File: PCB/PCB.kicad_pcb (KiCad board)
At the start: 2 copper layers, 45.6 x 12.2 mm, 9 parts, among them U1 STM8S003F3P, U2 PCB-USB-PWR-connector, U3 D168K

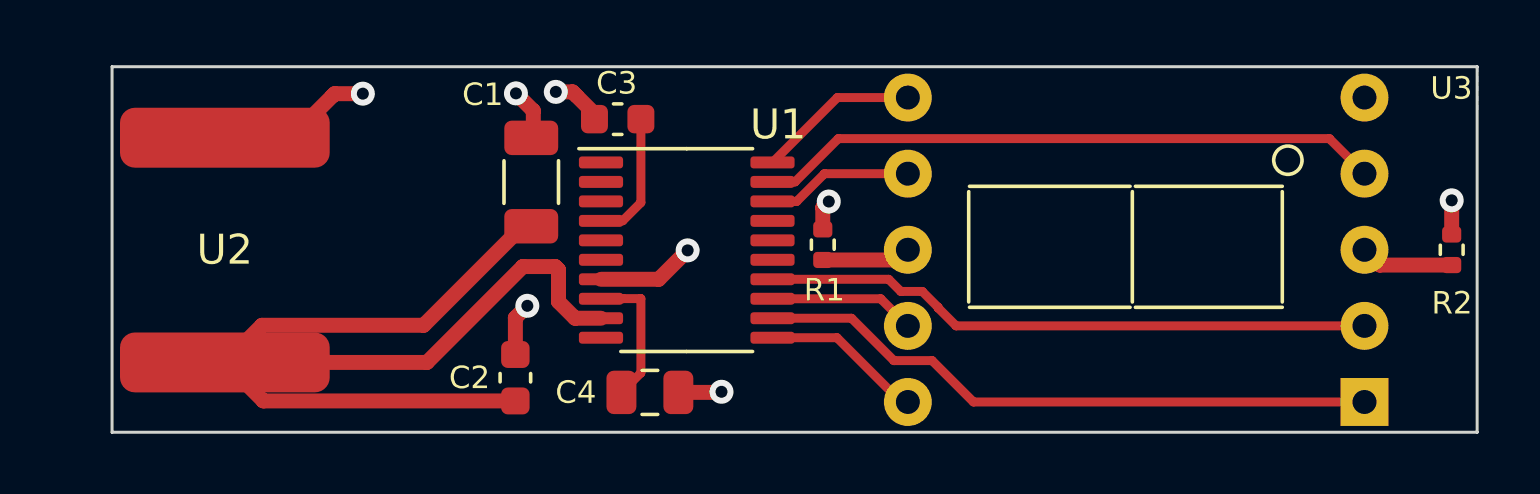
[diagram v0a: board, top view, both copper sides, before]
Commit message: PCB revision 0.11: correct decoupling capacitors, change IO routing, Schematic revision 0.12: change IO routing
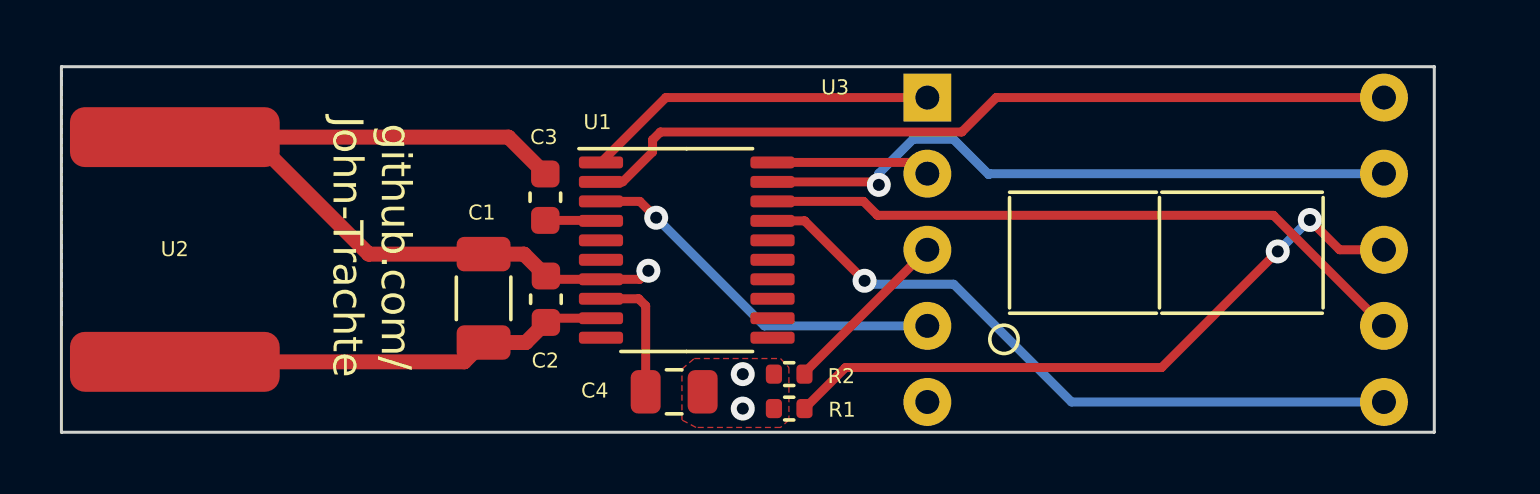
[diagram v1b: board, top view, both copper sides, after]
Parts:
- moved R2 22.5 mm to (153.0, 98.1), turned to 180 degrees
- moved U3 17.8 mm to (157.6, 88.9), turned to 0 degrees
- moved R1 5.58 mm to (153.0, 99.2), turned to 180 degrees
- moved C1 4.19 mm to (142.8, 95.6)
- moved C3 3.55 mm to (144.9, 92.2), turned to 90 degrees
- moved C2 2.81 mm to (144.9, 95.6)
- moved U2 1.67 mm to (132.5, 93.9)
- moved C4 0.81 mm to (149.2, 98.7)
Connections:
- net Net-(C4-Pad1) renamed /VCAP
- U1 pad 1: unconnected-(U1-Pad1) -> E
- U1 pad 11: G -> unconnected-(U1-Pad11)
- U1 pad 12: E -> unconnected-(U1-Pad12)
- U1 pad 13: F -> unconnected-(U1-Pad13)
- U1 pad 14: D -> unconnected-(U1-Pad14)
- U1 pad 17: unconnected-(U1-Pad17) -> B
- U1 pad 19: C -> F
- U1 pad 2: unconnected-(U1-Pad2) -> G
- U1 pad 20: B -> D
- U1 pad 3: unconnected-(U1-Pad3) -> C
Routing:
- net +5V: track 37.7 -> 14.8 mm
- net G: track 5.41 -> 27.5 mm
- net Net-(R1-Pad1): track 2.98 -> 22.4 mm, vias 0 -> 2
- net B: track 5.41 -> 22.9 mm, vias 0 -> 1
- net A: track 4.90 -> 22.1 mm
- net F: track 4.89 -> 21.8 mm, vias 0 -> 1
- net D: track 20.4 -> 5.32 mm
- net GND: track 17.3 -> 30.8 mm, vias 8 -> 3
- net E: track 20.9 -> 11.8 mm
- net C: track 20.8 -> 12.6 mm, vias 0 -> 1
- net Net-(R2-Pad1): track 3.12 -> 5.85 mm
- net /NRST: track 4.37 -> 1.86 mm
- added copper zone on F.Cu, net GND
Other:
- board size 45.6 x 12.2 mm -> 45.8 x 12.2 mm
- board text added: "github.com/ John-Trachte"

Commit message: Reflect MCU on dev board with original pinout
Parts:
- U1: value STM8S003F3P -> STM8S103F3P
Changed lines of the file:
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@@
       (effects (font (size 0.5 0.5) (thickness 0.125)))
     )
-    (fp_text value "STM8S003F3P" (at 0 4.2) (layer "F.Fab")
+    (fp_text value "STM8S103F3P" (at 0 4.2) (layer "F.Fab")
       (effects (font (size 1 1) (thickness 0.15)))
     )

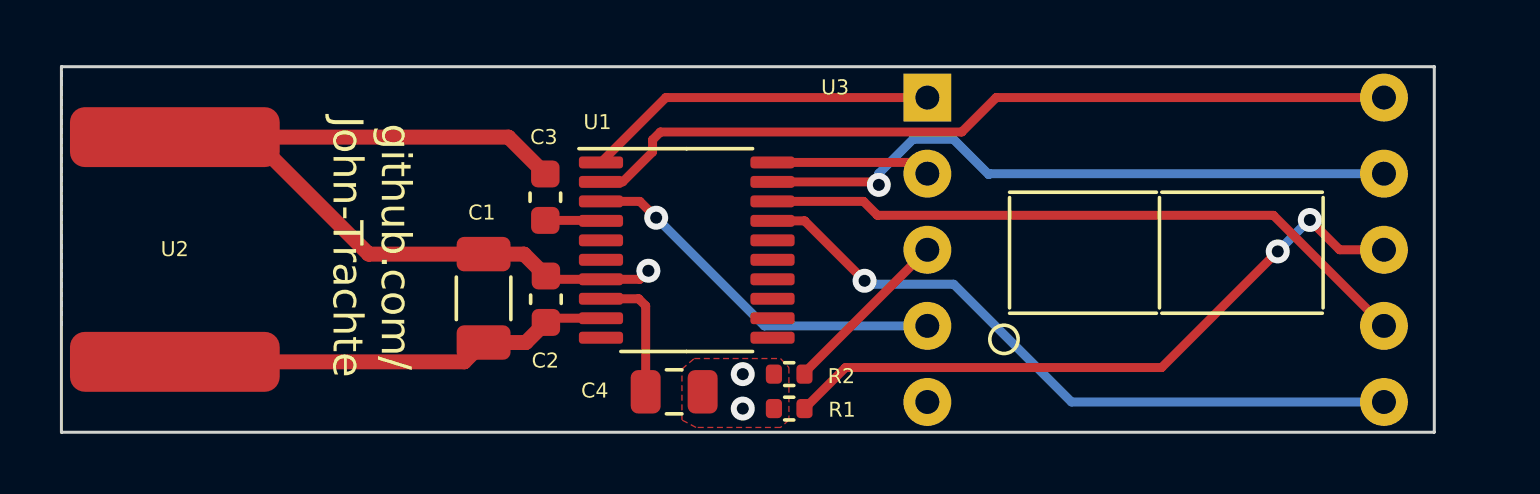
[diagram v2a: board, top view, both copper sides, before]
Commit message: Break out NRST for programming
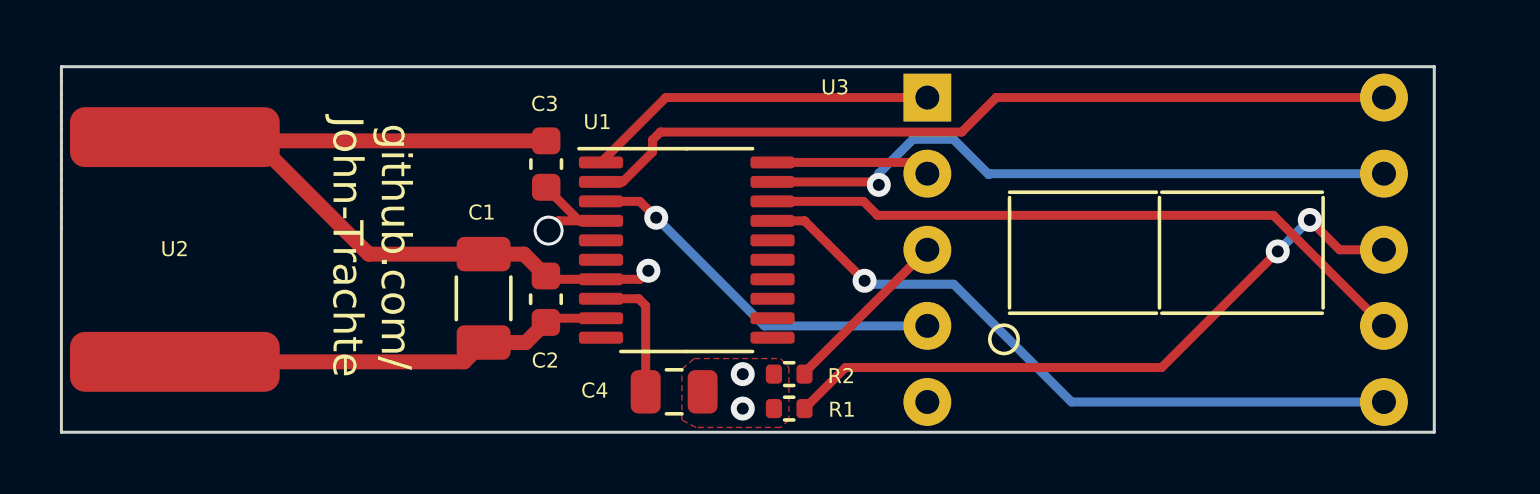
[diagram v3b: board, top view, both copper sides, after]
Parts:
- moved C3 1.11 mm to (144.9, 91.1)
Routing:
- net /NRST: track 1.86 -> 4.20 mm, vias 0 -> 1
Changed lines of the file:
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@@
   )
   (footprint "Capacitor_SMD:C_0603_1608Metric" (layer "F.Cu")
-    (at 144.89 92.195 90)
+    (at 144.92 91.09 90)
     (descr "Capacitor SMD 0603 (1608 Metric), square (rectangular) end terminal, IPC_7351 nominal, (Body size source: IPC-SM-782 page 76, https://www.pcb-3d.com/wordpress/wp-content/uploads/ipc-sm-782a_amendment_1_and_2.pdf), generated with kicad-footprint-generator")
     (tags "capacitor")
@@
     (effects (font (size 1 1) (thickness 0.15)))
   )
-  (segment (start 132.525 90.19) (end 143.66 90.19) (width 0.5) (layer "F.Cu") (net 1))
   (segment (start 145.02 94.935) (end 146.7475 94.935) (width 0.3) (layer "F.Cu") (net 1))
   (segment (start 148.045 94.935) (end 148.33 94.65) (width 0.3) (layer "F.Cu") (net 1))
   (segment (start 144.91 94.825) (end 145.02 94.935) (width 0.3) (layer "F.Cu") (net 1))
-  (segment (start 143.66 90.19) (end 144.89 91.42) (width 0.5) (layer "F.Cu") (net 1))
+  (segment (start 132.65 90.315) (end 132.525 90.19) (width 0.5) (layer "F.Cu") (net 1))
   (segment (start 135.09 90.19) (end 138.995 94.095) (width 0.5) (layer "F.Cu") (net 1))
   (segment (start 132.525 90.19) (end 135.09 90.19) (width 0.5) (layer "F.Cu") (net 1))
   (segment (start 146.7475 94.935) (end 148.045 94.935) (width 0.3) (layer "F.Cu") (net 1))
+  (segment (start 144.92 90.315) (end 132.65 90.315) (width 0.5) (layer "F.Cu") (net 1))
   (segment (start 138.995 94.095) (end 142.83 94.095) (width 0.5) (layer "F.Cu") (net 1))
   (segment (start 144.18 94.095) (end 144.91 94.825) (width 0.5) (layer "F.Cu") (net 1))
@@
   (via (at 148.33 94.65) (size 0.8) (drill 0.4) (layers "F.Cu" "B.Cu") (net 1))
   (via (at 151.48 98.1) (size 0.8) (drill 0.4) (layers "F.Cu" "B.Cu") (net 1))
-  (segment (start 144.89 92.97) (end 146.7325 92.97) (width 0.3) (layer "F.Cu") (net 2))
+  (segment (start 146.7475 92.985) (end 146.024283 92.985) (width 0.3) (layer "F.Cu") (net 2))
+  (segment (start 145.325 92.985) (end 145 93.31) (width 0.3) (layer "F.Cu") (net 2))
+  (segment (start 146.024283 92.985) (end 144.92 91.880717) (width 0.3) (layer "F.Cu") (net 2))
+  (segment (start 146.7475 92.985) (end 145.325 92.985) (width 0.3) (layer "F.Cu") (net 2))
+  (segment (start 144.92 91.880717) (end 144.92 91.865) (width 0.3) (layer "F.Cu") (net 2))
   (segment (start 146.7325 92.97) (end 146.7475 92.985) (width 0.3) (layer "F.Cu") (net 2))
+  (via (at 145 93.31) (size 1) (drill 0.8) (layers "F.Cu" "B.Cu") (net 2))
   (segment (start 165.459511 97.880489) (end 154.909511 97.880489) (width 0.3) (layer "F.Cu") (net 3))
   (segment (start 169.335023 94.004977) (end 165.459511 97.880489) (width 0.3) (layer "F.Cu") (net 3))

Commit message: Add UART header
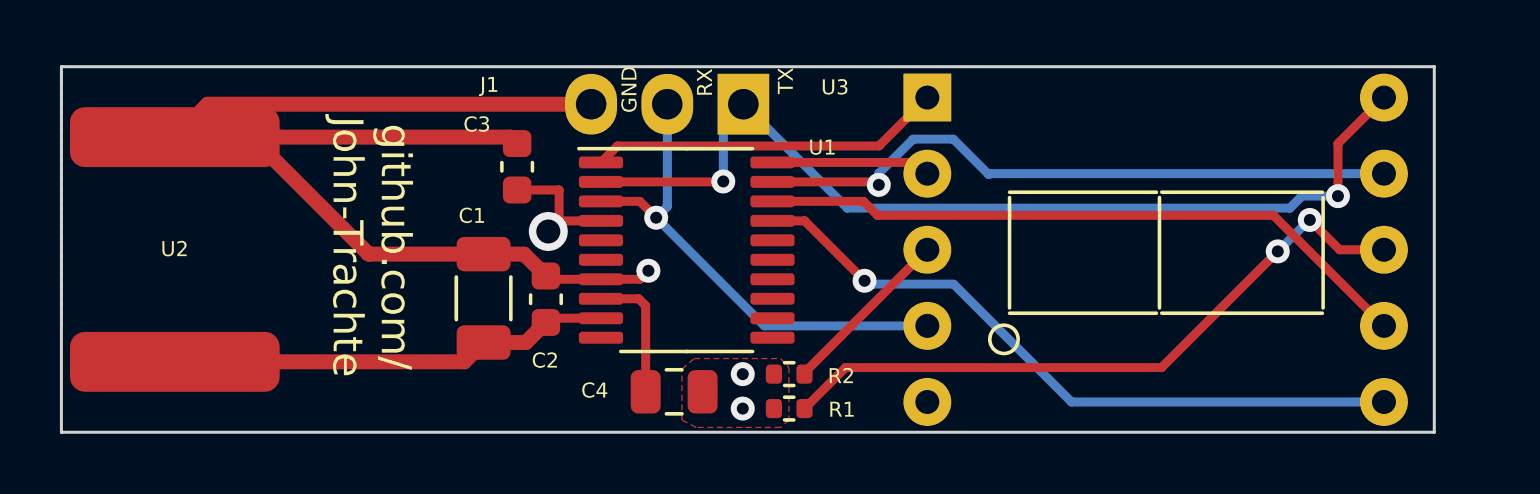
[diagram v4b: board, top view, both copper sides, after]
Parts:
- added J1: UART, Connector:FanPinHeader_1x03_P2.54mm_Vertical, F.Cu at (151.5, 89.1)
- moved C3 0.97 mm to (143.9, 91.2)
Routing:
- net GND: track 30.3 -> 43.8 mm
- net G: track 27.5 -> 32.3 mm, vias 0 -> 2
- net C: track 12.6 -> 16.6 mm
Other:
- board text added: "GND"
- board text added: "RX"
- board text added: "TX"
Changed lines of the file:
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@@
     (property "Sheetname" "")
     (attr smd)
-    (fp_text reference "U1" (at -2.98 -4.27) (layer "F.SilkS")
+    (fp_text reference "U1" (at 4.53 -3.42) (layer "F.SilkS")
       (effects (font (size 0.5 0.5) (thickness 0.125)))
     )
@@
     (property "Sheetname" "")
     (attr smd)
-    (fp_text reference "C1" (at 2.86 -0.06) (layer "F.SilkS")
+    (fp_text reference "C1" (at 2.75 -0.38) (layer "F.SilkS")
       (effects (font (size 0.5 0.5) (thickness 0.125)))
     )
@@
       (net 1 "GND") (pintype "passive"))
     (model "${KICAD6_3DMODEL_DIR}/Resistor_SMD.3dshapes/R_0402_1005Metric.wrl"
+      (offset (xyz 0 0 0))
+      (scale (xyz 1 1 1))
+      (rotate (xyz 0 0 0))
+    )
+  )
+  (footprint "Connector:FanPinHeader_1x03_P2.54mm_Vertical" (layer "F.Cu")
+    (at 151.5 89.092 180)
+    (descr "3-pin CPU fan Through hole pin header, see http://www.formfactors.org/developer%5Cspecs%5Crev1_2_public.pdf")
+    (tags "pin header 3-pin CPU fan")
+    (property "Sheetfile" "PCB.kicad_sch")
+    (property "Sheetname" "")
+    (attr through_hole)
+    (fp_text reference "J1" (at 8.47 0.642) (layer "F.SilkS")
+      (effects (font (size 0.5 0.5) (thickness 0.125)))
+    )
+    (fp_text value "UART" (at 2.55 2.032) (layer "F.Fab")
+      (effects (font (size 1 1) (thickness 0.15)))
+    )
+    (pad "1" thru_hole rect (at 0 0 270) (size 2.03 1.73) (drill 1.02) (layers *.Cu *.Mask)
+      (net 13 "G") (pinfunction "Pin_1") (pintype "passive"))
+    (pad "2" thru_hole oval (at 2.54 0 270) (size 2.03 1.73) (drill 1.02) (layers *.Cu *.Mask)
+      (net 16 "C") (pinfunction "Pin_2") (pintype "passive"))
+    (pad "3" thru_hole oval (at 5.08 0 270) (size 2.03 1.73) (drill 1.02) (layers *.Cu *.Mask)
+      (net 1 "GND") (pinfunction "Pin_3") (pintype "passive"))
+    (model "${KICAD6_3DMODEL_DIR}/Connector.3dshapes/FanPinHeader_1x03_P2.54mm_Vertical.wrl"
       (offset (xyz 0 0 0))
       (scale (xyz 1 1 1))
@@
   )
   (footprint "Capacitor_SMD:C_0603_1608Metric" (layer "F.Cu")
-    (at 144.92 91.09 90)
+    (at 143.95 91.18 90)
     (descr "Capacitor SMD 0603 (1608 Metric), square (rectangular) end terminal, IPC_7351 nominal, (Body size source: IPC-SM-782 page 76, https://www.pcb-3d.com/wordpress/wp-content/uploads/ipc-sm-782a_amendment_1_and_2.pdf), generated with kicad-footprint-generator")
     (tags "capacitor")
@@
     (property "Sheetname" "")
     (attr smd)
-    (fp_text reference "C3" (at 2.005 -0.05 180) (layer "F.SilkS")
+    (fp_text reference "C3" (at 1.41 -1.34 180) (layer "F.SilkS")
       (effects (font (size 0.5 0.5) (thickness 0.125)))
     )
@@
   )
   (gr_rect (start 128.74 87.84) (end 174.56 100.04) (layer "Edge.Cuts") (width 0.1) (fill none))
+  (gr_text "TX" (at 152.92 88.31 90) (layer "F.SilkS")
+    (effects (font (size 0.5 0.5) (thickness 0.125)))
+  )
   (gr_text "github.com/\nJohn-Trachte" (at 139.09 93.85 270) (layer "F.SilkS")
     (effects (font (size 1 1) (thickness 0.15)))
+  )
+  (gr_text "GND" (at 147.7 88.6 90) (layer "F.SilkS")
+    (effects (font (size 0.5 0.5) (thickness 0.125)))
+  )
+  (gr_text "RX" (at 150.22 88.37 90) (layer "F.SilkS")
+    (effects (font (size 0.5 0.5) (thickness 0.125)))
   )
   (segment (start 145.02 94.935) (end 146.7475 94.935) (width 0.3) (layer "F.Cu") (net 1))
   (segment (start 148.045 94.935) (end 148.33 94.65) (width 0.3) (layer "F.Cu") (net 1))
   (segment (start 144.91 94.825) (end 145.02 94.935) (width 0.3) (layer "F.Cu") (net 1))
-  (segment (start 132.65 90.315) (end 132.525 90.19) (width 0.5) (layer "F.Cu") (net 1))
+  (segment (start 146.42 89.092) (end 133.623 89.092) (width 0.5) (layer "F.Cu") (net 1))
+  (segment (start 132.525 90.19) (end 143.735 90.19) (width 0.5) (layer "F.Cu") (net 1))
+  (segment (start 133.623 89.092) (end 132.525 90.19) (width 0.5) (layer "F.Cu") (net 1))
+  (segment (start 143.735 90.19) (end 143.95 90.405) (width 0.5) (layer "F.Cu") (net 1))
   (segment (start 135.09 90.19) (end 138.995 94.095) (width 0.5) (layer "F.Cu") (net 1))
   (segment (start 132.525 90.19) (end 135.09 90.19) (width 0.5) (layer "F.Cu") (net 1))
   (segment (start 146.7475 94.935) (end 148.045 94.935) (width 0.3) (layer "F.Cu") (net 1))
-  (segment (start 144.92 90.315) (end 132.65 90.315) (width 0.5) (layer "F.Cu") (net 1))
   (segment (start 138.995 94.095) (end 142.83 94.095) (width 0.5) (layer "F.Cu") (net 1))
   (segment (start 144.18 94.095) (end 144.91 94.825) (width 0.5) (layer "F.Cu") (net 1))
@@
   (via (at 148.33 94.65) (size 0.8) (drill 0.4) (layers "F.Cu" "B.Cu") (net 1))
   (via (at 151.48 98.1) (size 0.8) (drill 0.4) (layers "F.Cu" "B.Cu") (net 1))
-  (segment (start 146.7475 92.985) (end 146.024283 92.985) (width 0.3) (layer "F.Cu") (net 2))
-  (segment (start 145.325 92.985) (end 145 93.31) (width 0.3) (layer "F.Cu") (net 2))
-  (segment (start 146.024283 92.985) (end 144.92 91.880717) (width 0.3) (layer "F.Cu") (net 2))
-  (segment (start 146.7475 92.985) (end 145.325 92.985) (width 0.3) (layer "F.Cu") (net 2))
-  (segment (start 144.92 91.880717) (end 144.92 91.865) (width 0.3) (layer "F.Cu") (net 2))
-  (segment (start 146.7325 92.97) (end 146.7475 92.985) (width 0.3) (layer "F.Cu") (net 2))
-  (via (at 145 93.31) (size 1) (drill 0.8) (layers "F.Cu" "B.Cu") (net 2))
+  (segment (start 145.35 91.96) (end 145.345 91.955) (width 0.3) (layer "F.Cu") (net 2))
+  (segment (start 145.345 92.985) (end 146.7475 92.985) (width 0.3) (layer "F.Cu") (net 2))
+  (segment (start 145.345 91.955) (end 143.95 91.955) (width 0.3) (layer "F.Cu") (net 2))
+  (segment (start 145.345 92.985) (end 145.35 92.98) (width 0.3) (layer "F.Cu") (net 2))
+  (segment (start 144.99 93.34) (end 145.345 92.985) (width 0.3) (layer "F.Cu") (net 2))
+  (segment (start 145.35 92.98) (end 145.35 91.96) (width 0.3) (layer "F.Cu") (net 2))
+  (via (at 144.99 93.34) (size 1.3) (drill 0.8) (layers "F.Cu" "B.Cu") (net 2))
   (segment (start 165.459511 97.880489) (end 154.909511 97.880489) (width 0.3) (layer "F.Cu") (net 3))
   (segment (start 169.335023 94.004977) (end 165.459511 97.880489) (width 0.3) (layer "F.Cu") (net 3))
@@
   (segment (start 157.265 91.035) (end 157.64 91.41) (width 0.3) (layer "F.Cu") (net 5))
   (segment (start 152.4725 91.035) (end 157.265 91.035) (width 0.3) (layer "F.Cu") (net 5))
-  (segment (start 148.9125 88.87) (end 157.64 88.87) (width 0.3) (layer "F.Cu") (net 6))
-  (segment (start 146.7475 91.035) (end 148.9125 88.87) (width 0.3) (layer "F.Cu") (net 6))
+  (segment (start 156.02452 90.48548) (end 157.64 88.87) (width 0.3) (layer "F.Cu") (net 6))
+  (segment (start 147.29702 90.48548) (end 156.02452 90.48548) (width 0.3) (layer "F.Cu") (net 6))
+  (segment (start 146.7475 91.035) (end 147.29702 90.48548) (width 0.3) (layer "F.Cu") (net 6))
   (segment (start 152.4725 91.685) (end 155.9205 91.685) (width 0.3) (layer "F.Cu") (net 7))
   (segment (start 155.9205 91.685) (end 156.02 91.7845) (width 0.3) (layer "F.Cu") (net 7))
@@
   (segment (start 158.51 90.26) (end 159.69 91.44) (width 0.3) (layer "B.Cu") (net 7))
   (segment (start 159.72 91.41) (end 172.88 91.41) (width 0.3) (layer "B.Cu") (net 7))
-  (segment (start 148.47 90.685717) (end 147.470717 91.685) (width 0.3) (layer "F.Cu") (net 13))
-  (segment (start 158.789511 90.019511) (end 148.730489 90.019511) (width 0.3) (layer "F.Cu") (net 13))
-  (segment (start 147.470717 91.685) (end 146.7475 91.685) (width 0.3) (layer "F.Cu") (net 13))
-  (segment (start 148.730489 90.019511) (end 148.47 90.28) (width 0.3) (layer "F.Cu") (net 13))
-  (segment (start 159.939022 88.87) (end 158.789511 90.019511) (width 0.3) (layer "F.Cu") (net 13))
-  (segment (start 148.47 90.28) (end 148.47 90.685717) (width 0.3) (layer "F.Cu") (net 13))
-  (segment (start 172.88 88.87) (end 159.939022 88.87) (width 0.3) (layer "F.Cu") (net 13))
+  (segment (start 171.344847 90.405153) (end 172.88 88.87) (width 0.3) (layer "F.Cu") (net 13))
+  (segment (start 171.344847 92.1595) (end 171.344847 90.405153) (width 0.3) (layer "F.Cu") (net 13))
+  (segment (start 150.815 91.685) (end 150.83 91.67) (width 0.3) (layer "F.Cu") (net 13))
+  (segment (start 146.7475 91.685) (end 150.815 91.685) (width 0.3) (layer "F.Cu") (net 13))
+  (via (at 171.344847 92.1595) (size 0.8) (drill 0.4) (layers "F.Cu" "B.Cu") (net 13))
+  (via (at 150.83 91.67) (size 0.8) (drill 0.4) (layers "F.Cu" "B.Cu") (net 13))
+  (segment (start 169.740519 92.559511) (end 170.14053 92.1595) (width 0.3) (layer "B.Cu") (net 13))
+  (segment (start 170.14053 92.1595) (end 171.344847 92.1595) (width 0.3) (layer "B.Cu") (net 13))
+  (segment (start 150.83 91.67) (end 150.83 89.762) (width 0.3) (layer "B.Cu") (net 13))
+  (segment (start 154.967511 92.559511) (end 169.740519 92.559511) (width 0.3) (layer "B.Cu") (net 13))
+  (segment (start 150.83 89.762) (end 151.5 89.092) (width 0.3) (layer "B.Cu") (net 13))
+  (segment (start 151.5 89.092) (end 154.967511 92.559511) (width 0.3) (layer "B.Cu") (net 13))
   (segment (start 169.190489 92.800489) (end 172.88 96.49) (width 0.3) (layer "F.Cu") (net 14))
   (segment (start 155.51053 92.335) (end 155.976019 92.800489) (width 0.3) (layer "F.Cu") (net 14))
@@
   (segment (start 148.59 92.88) (end 152.2 96.49) (width 0.3) (layer "B.Cu") (net 16))
   (segment (start 152.2 96.49) (end 157.64 96.49) (width 0.3) (layer "B.Cu") (net 16))
+  (segment (start 148.96 92.51) (end 148.96 89.092) (width 0.3) (layer "B.Cu") (net 16))
+  (segment (start 148.59 92.88) (end 148.96 92.51) (width 0.3) (layer "B.Cu") (net 16))
   (segment (start 148.24 95.82) (end 148.005 95.585) (width 0.3) (layer "F.Cu") (net 22))
   (segment (start 148.24 98.69) (end 148.24 95.82) (width 0.3) (layer "F.Cu") (net 22))
